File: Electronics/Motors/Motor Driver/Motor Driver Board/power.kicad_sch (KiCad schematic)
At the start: 22 parts, among them IC5 TPS54295PWPR, J2 Screw_Terminal_01x02

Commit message: PCB Schematic progress
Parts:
- added J10, J11, J9: Conn_01x02_Pin, Connector_PinHeader_2.54mm:PinHeader_1x02_P2.54mm_Vertical, symbol Connector:Conn_01x02_Pin
- C8, C9: footprint Capacitor_SMD:C_0402_1005Metric -> Capacitor_SMD:C_0603_1608Metric
- D2, D3: value LED_R -> Green
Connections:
- net +5V: now also J10.1 (Pin_1), J11.1 (Pin_1), J9.1 (Pin_1)
- net GND: now also J10.2 (Pin_2), J11.2 (Pin_2), J9.2 (Pin_2)
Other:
- note added: "5V Fan Headers"
- note removed: "LEDs for each voltage rail"
- moved on the sheet: C10, C11, C3, C4, C5, C6, C7, C8, C9, D1, D2, D3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

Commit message: PCB Schematics finished
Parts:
- renumbered IC5 to IC201, J9 to J202, J10 to J203, J11 to J204

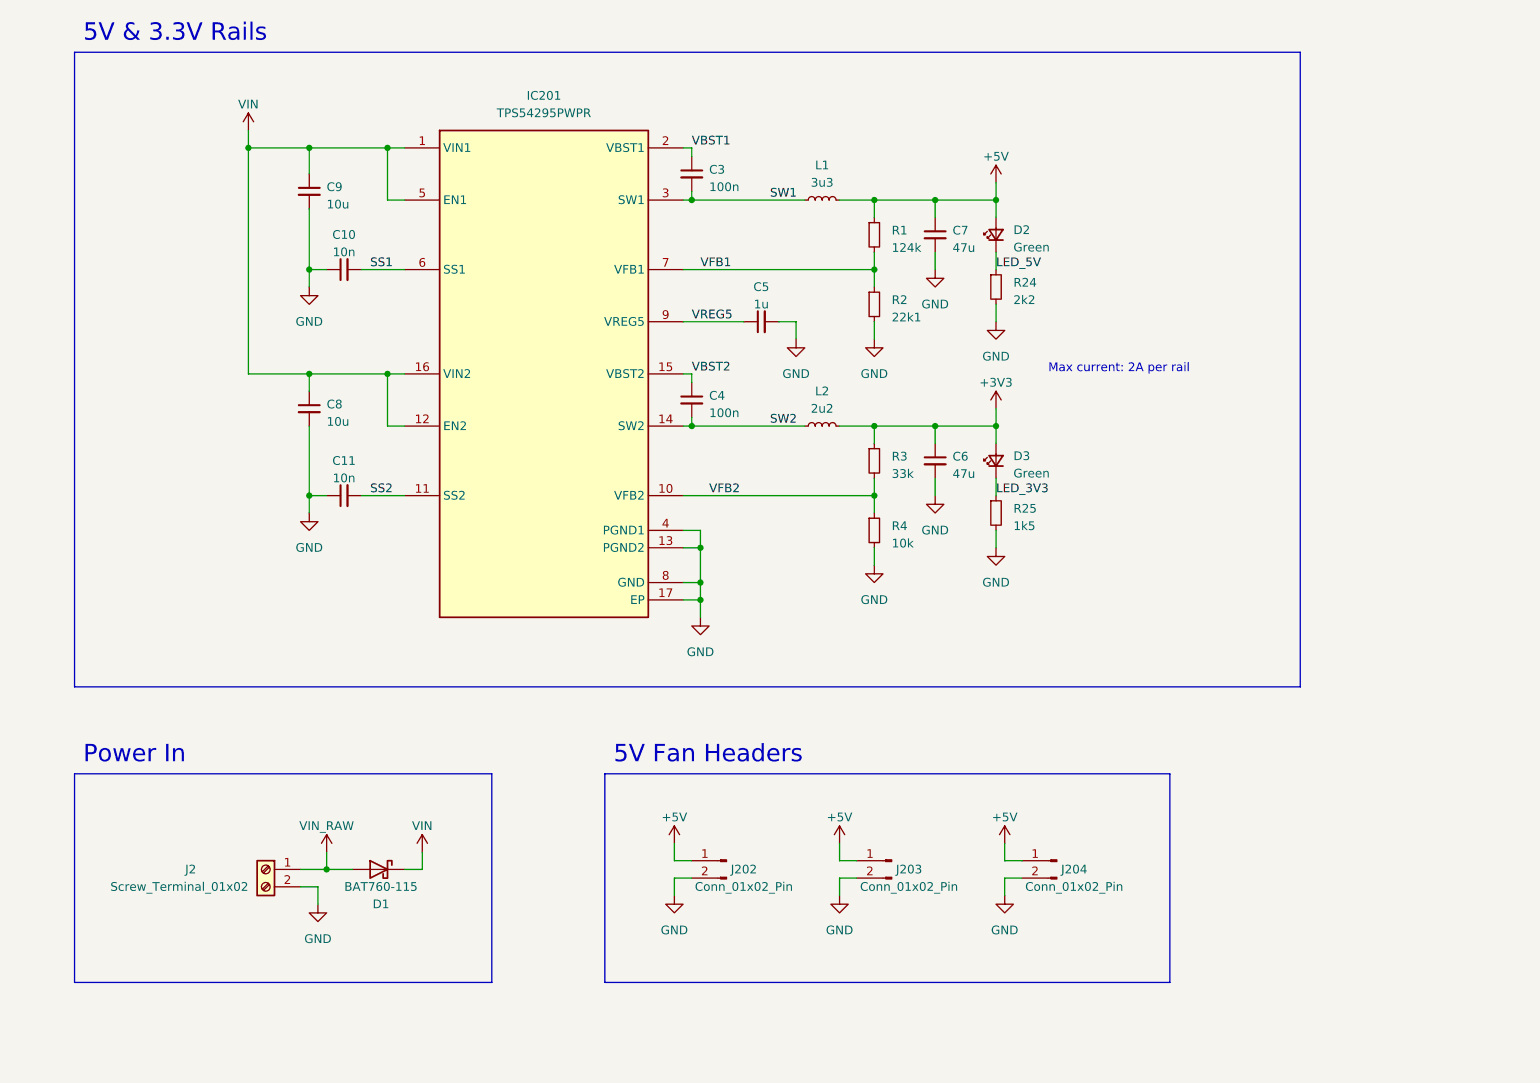
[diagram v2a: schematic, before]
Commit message: Schematic updates
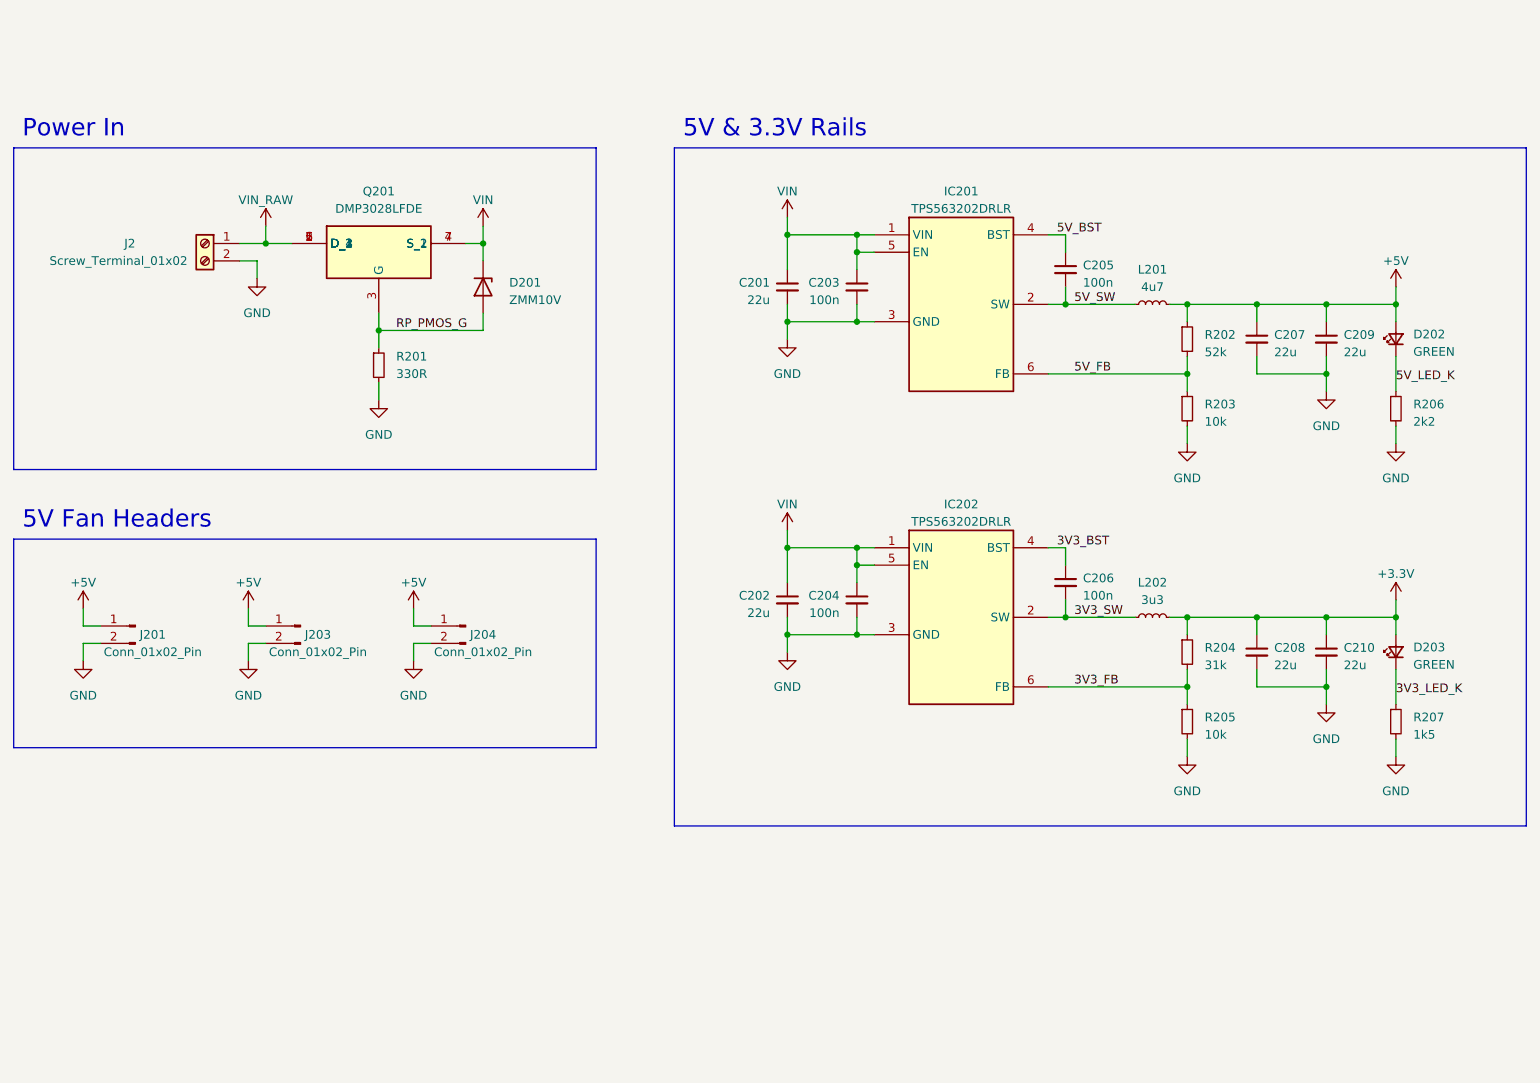
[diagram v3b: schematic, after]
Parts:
- removed C10, C11: 10n, Capacitor_SMD:C_0402_1005Metric, symbol Device:C_Small
- removed C3, C4: 100n, Capacitor_SMD:C_0402_1005Metric, symbol Device:C_Small
- removed C5: 1u, Capacitor_SMD:C_0402_1005Metric, symbol Device:C_Small
- removed C6, C7: 47u, Capacitor_SMD:C_0805_2012Metric, symbol Device:C_Small
- removed C8, C9: 10u, Capacitor_SMD:C_0603_1608Metric, symbol Device:C_Small
- removed D1: BAT760-115, Diode_SMD:D_SOD-323, symbol Device:D_Schottky
- removed D2, D3: Green, LED_SMD:LED_0603_1608Metric, symbol Device:LED_Small
- removed IC201: TPS54295PWPR, SOP65P640X120-17N, symbol TPS54295PWPR:TPS54295PWPR
- removed J202: Conn_01x02_Pin, Connector_PinHeader_2.54mm:PinHeader_1x02_P2.54mm_Vertical, symbol Connector:Conn_01x02_Pin
- removed L1: 3u3, MSL Footprints:29332C, symbol Device:L_Small
- removed L2: 2u2, MSL Footprints:29222C, symbol Device:L_Small
- removed R1: 124k, Resistor_SMD:R_0402_1005Metric, symbol Device:R_Small
- removed R2: 22k1, Resistor_SMD:R_0402_1005Metric, symbol Device:R_Small
- removed R24: 2k2, Resistor_SMD:R_0402_1005Metric, symbol Device:R_Small
- removed R25: 1k5, Resistor_SMD:R_0402_1005Metric, symbol Device:R_Small
- removed R3: 33k, Resistor_SMD:R_0402_1005Metric, symbol Device:R_Small
- removed R4: 10k, Resistor_SMD:R_0402_1005Metric, symbol Device:R_Small
- added C201, C202, C207, C208, C209, C210: 22u, Capacitor_SMD:C_0603_1608Metric, symbol Device:C_Small
- added C203, C204, C205, C206: 100n, Capacitor_SMD:C_0402_1005Metric, symbol Device:C_Small
- added D201: ZMM10V, Diode_SMD:D_MiniMELF, symbol Diode:ZMMxx
- added D202, D203: GREEN, LED_SMD:LED_0603_1608Metric, symbol Device:LED_Small
- added IC201, IC202: TPS563202DRLR, MSL Footprints:SOTFL50P160X60-6N, symbol TPS563202DRLR:TPS563202DRLR
- added J201: Conn_01x02_Pin, Connector_PinHeader_2.54mm:PinHeader_1x02_P2.54mm_Vertical, symbol Connector:Conn_01x02_Pin
- added L201: 4u7, Inductor_SMD:L_Chilisin_BMRA00040420, symbol Device:L_Small
- added L202: 3u3, Inductor_SMD:L_Chilisin_BMRA00040420, symbol Device:L_Small
- added Q201: DMP3028LFDE, 101 Footprints:DMP2066UFDE7, symbol DMP3028LFDE-7:DMP3028LFDE
- added R201: 330R, Resistor_SMD:R_0402_1005Metric, symbol Device:R_Small
- added R202: 52k, Resistor_SMD:R_0402_1005Metric, symbol Device:R_Small
- added R203, R205: 10k, Resistor_SMD:R_0402_1005Metric, symbol Device:R_Small
- added R204: 31k, Resistor_SMD:R_0402_1005Metric, symbol Device:R_Small
- added R206: 2k2, Resistor_SMD:R_0402_1005Metric, symbol Device:R_Small
- added R207: 1k5, Resistor_SMD:R_0402_1005Metric, symbol Device:R_Small
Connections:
- net +5V: now also C207.1, C209.1, D202.2 (A), J201.1 (Pin_1), L201.2, R202.1
- net GND: now also C201.2, C202.2, C203.2, C204.2, C207.2, C208.2, C209.2, C210.2, IC201.3 (GND), IC202.3 (GND), J201.2 (Pin_2), R201.2, R203.2, R205.2, R206.2, R207.2
- net VIN: now also C201.1, C202.1, C203.1, C204.1, D201.1 (K), IC201.1 (VIN), IC201.5 (EN), IC202.1 (VIN), IC202.5 (EN), Q201.4 (S_1), Q201.7 (S_2)
- net VIN_RAW: now also Q201.1 (D_1), Q201.2 (D_2), Q201.5 (D_3), Q201.6 (D_4)
- new net +3.3V: C208.1, C210.1, D203.2 (A), L202.2, R204.1
- new net 3V3_BST: C206.1, IC202.4 (BST)
- new net 3V3_FB: IC202.6 (FB), R204.2, R205.1
- new net 3V3_LED_K: D203.1 (K), R207.1
- new net 3V3_SW: C206.2, IC202.2 (SW), L202.1
- new net 5V_BST: C205.1, IC201.4 (BST)
- new net 5V_FB: IC201.6 (FB), R202.2, R203.1
- new net 5V_LED_K: D202.1 (K), R206.1
- new net 5V_SW: C205.2, IC201.2 (SW), L201.1
- new net RP_PMOS_G: D201.2 (A), Q201.3 (G), R201.1
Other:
- note removed: "Max current: 2A per rail"

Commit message: PCB layout progress, spice simulations for power board
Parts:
- Q201: footprint 101 Footprints:DMP2066UFDE7 -> MSL Footprints:DMP2066UFDE7
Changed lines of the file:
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@@
       (effects (font (size 1.27 1.27)))
     )
-    (property "Footprint" "101 Footprints:DMP2066UFDE7" (at 116.84 149.53 0)
+    (property "Footprint" "MSL Footprints:DMP2066UFDE7" (at 116.84 149.53 0)
       (effects (font (size 1.27 1.27)) (justify left top) hide)
     )

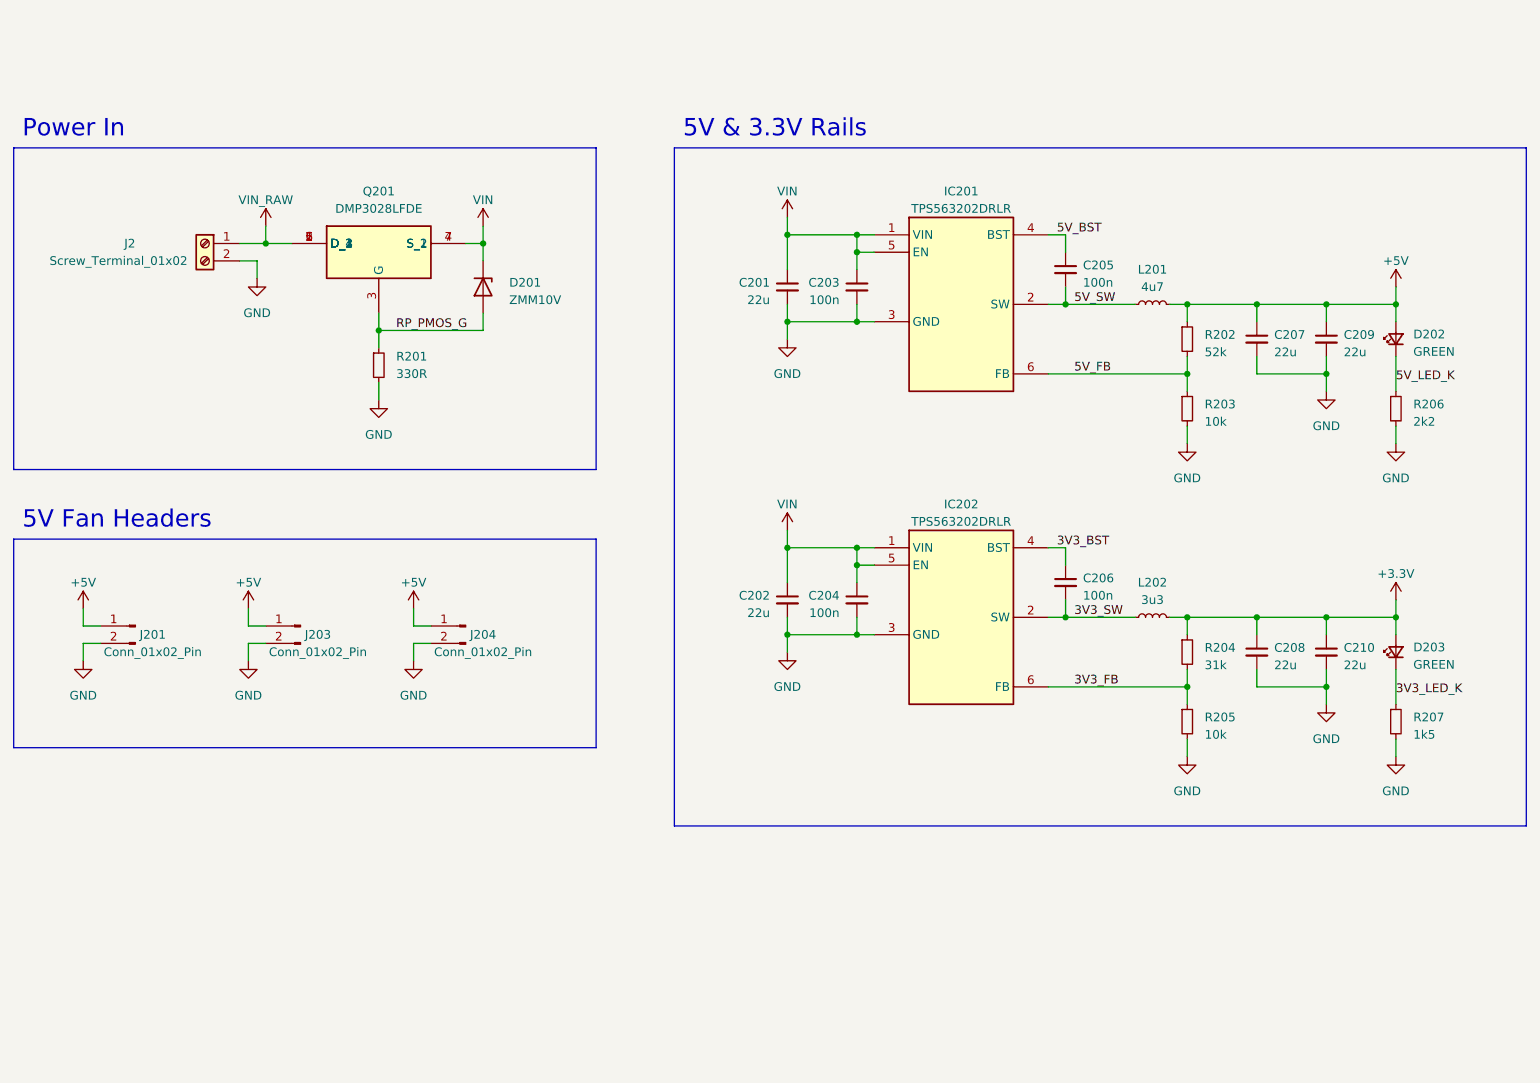
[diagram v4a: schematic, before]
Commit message: Gateway board layout complete and routing begun
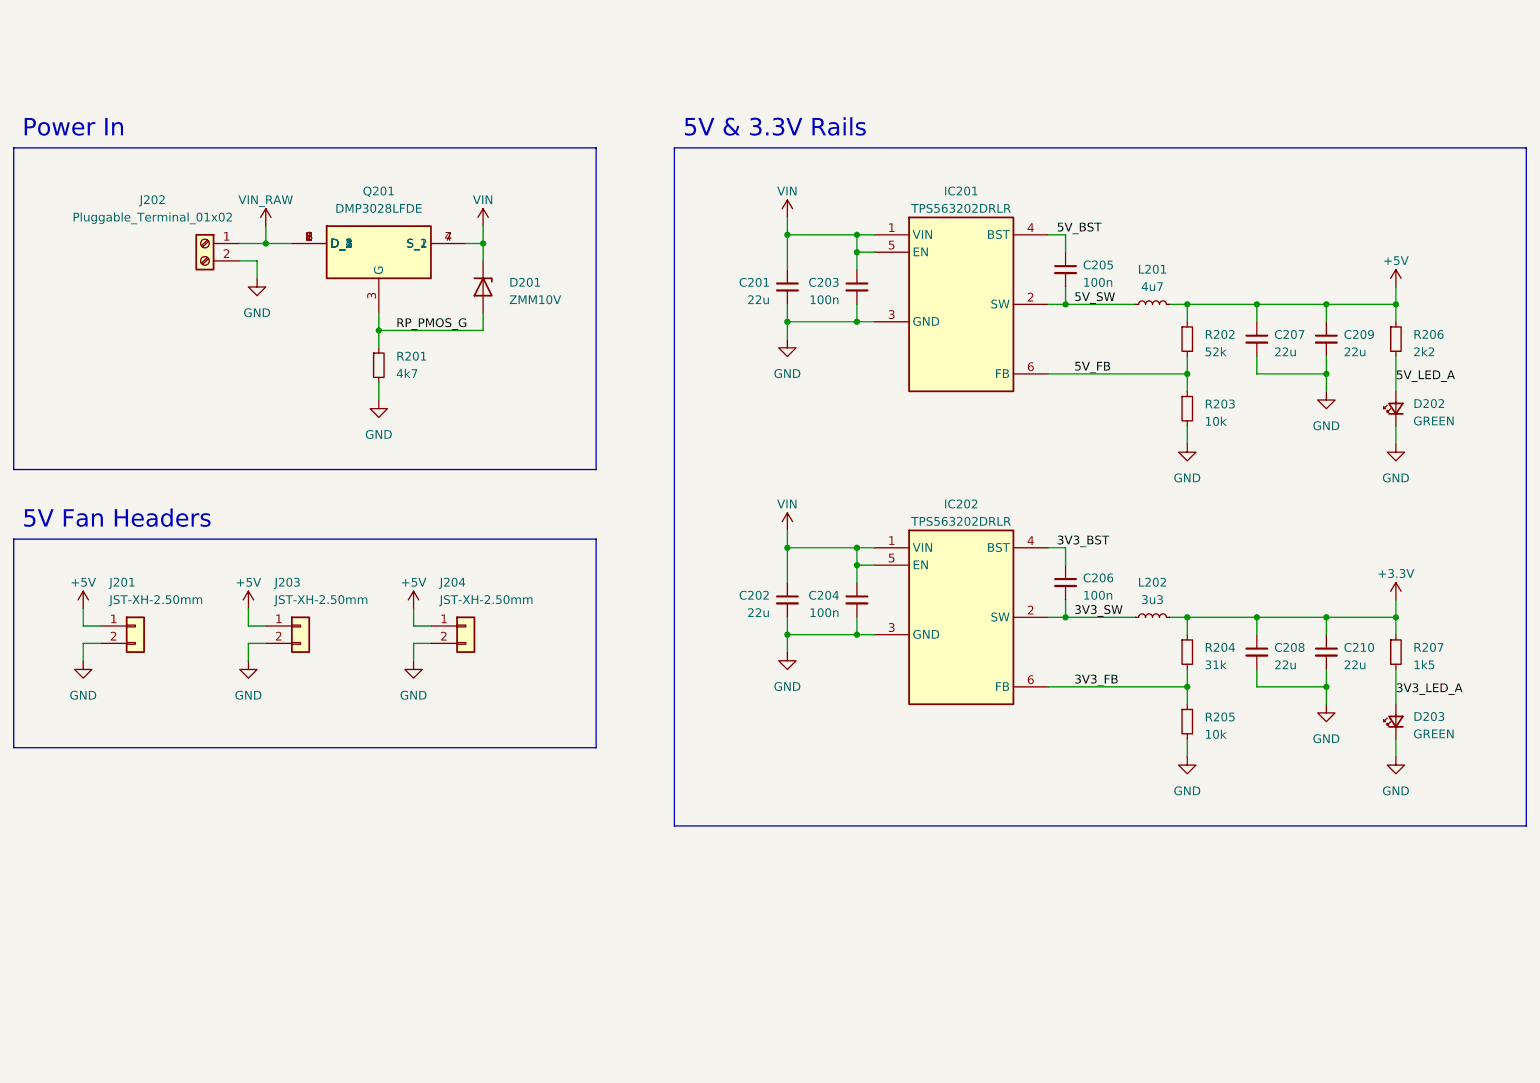
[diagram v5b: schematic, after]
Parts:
- removed J2: Screw_Terminal_01x02, TerminalBlock:TerminalBlock_bornier-2_P5.08mm, symbol Connector:Screw_Terminal_01x02
- removed J201, J203, J204: Conn_01x02_Pin, Connector_PinHeader_2.54mm:PinHeader_1x02_P2.54mm_Vertical, symbol Connector:Conn_01x02_Pin
- added J201, J203, J204: JST-XH-2.50mm, Connector_JST:JST_XH_B2B-XH-A_1x02_P2.50mm_Vertical, symbol MSL_Symbols:JST_2.5mm_1x2
- added J202: Pluggable_Terminal_01x02, MSL Footprints:Pluggable_terminal-2_P5.08mm, symbol MSL_Symbols:Pluggable_Terminal_01x02
- R201: value 330R -> 4k7
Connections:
- net +3.3V: now also R207.1; no longer D203.2 (A)
- net +5V: now also R206.1, J201.1 (Pin_1), J203.1 (Pin_1), J204.1 (Pin_1); no longer D202.2 (A)
- net GND: now also D202.1 (K), D203.1 (K), J201.2 (Pin_2), J202.2 (Pin_2), J203.2 (Pin_2), J204.2 (Pin_2); no longer R206.2, R207.2
- net VIN_RAW: now also Q201.8 (D_5), J202.1 (Pin_1)
- removed net 3V3_LED_K: D203.1 (K), R207.1
- removed net 5V_LED_K: D202.1 (K), R206.1
- new net 3V3_LED_A: D203.2 (A), R207.2
- new net 5V_LED_A: D202.2 (A), R206.2
